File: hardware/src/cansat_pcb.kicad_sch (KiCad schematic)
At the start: 0 parts

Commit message: app advanced
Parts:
- added U1: XIAO-nRF52840-SMD, Seeed_Studio_XIAO_Series:XIAO-nRF52840-SMD, symbol Seeed_Studio_XIAO_Series-20240814:XIAO-nRF52840-SMD
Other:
- company: (none) -> Hydro Vinci
- title: (none) -> Cansat_pcb
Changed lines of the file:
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@@
 	(generator "eeschema")
 	(generator_version "9.0")
-	(paper "A4")
+	(paper "A3")
+	(title_block
+		(title "Cansat_pcb")
+		(date "2026-02-22")
+		(rev "Enzo Morin")
+		(company "Hydro Vinci")
+		(comment 1 "1st layer of the pcb in the cansat")
+	)
+	(rectangle
+		(start 12.7 12.7)
+		(end 151.13 142.24)
+		(stroke
+			(width 0)
+			(type default)
+			(color 194 0 0 1)
+		)
+		(fill
+			(type none)
+		)
+	)
+	(label "actuators/indicators"
+		(at 167.64 154.94 0)
+		(effects
+			(font
+				(size 4.27 4.27)
+			)
+			(justify left bottom)
+		)
+	)
+	(label "Main-part_microcontroler"
+		(at 15.24 21.59 0)
+		(effects
+			(font
+				(size 4.27 4.27)
+			)
+			(justify left bottom)
+		)
+	)
+	(label "storage and radio"
+		(at 226.06 25.4 0)
+		(effects
+			(font
+				(size 4.27 4.27)
+			)
+			(justify left bottom)
+		)
+	)
+	(label "alimentation"
+		(at 157.48 25.4 0)
+		(effects
+			(font
+				(size 4.27 4.27)
+			)
+			(justify left bottom)
+		)
+	)
+	(label "sensors"
+		(at 21.59 154.94 0)
+		(effects
+			(font
+				(size 4.27 4.27)
+			)
+			(justify left bottom)
+		)
+	)
+	(symbol
+		(lib_id "Seeed_Studio_XIAO_Series-20240814:XIAO-nRF52840-SMD")
+		(at 64.77 74.93 0)
+		(unit 1)
+		(exclude_from_sim no)
+		(in_bom yes)
+		(on_board yes)
+		(dnp no)
+		(fields_autoplaced yes)
+		(property "Reference" "U1"
+			(at 73.2633 49.53 0)
+			(effects
+				(font
+					(size 1.27 1.27)
+				)
+				(justify left)
+			)
+		)
+		(property "Value" "XIAO-nRF52840-SMD"
+			(at 73.2633 52.07 0)
+			(effects
+				(font
+					(size 1.27 1.27)
+				)
+				(justify left)
+			)
+		)
+		(property "Footprint" "Seeed_Studio_XIAO_Series:XIAO-nRF52840-SMD"
+			(at 55.88 69.85 0)
+			(effects
+				(font
+					(size 1.27 1.27)
+				)
+				(hide yes)
+			)
+		)
+		(property "Datasheet" ""
+			(at 55.88 69.85 0)
+			(effects
+				(font
+					(size 1.27 1.27)
+				)
+				(hide yes)
+			)
+		)
+		(property "Description" ""
+			(at 64.77 74.93 0)
+			(effects
+				(font
+					(size 1.27 1.27)
+				)
+				(hide yes)
+			)
+		)
+		(pin "18"
+		)
+		(pin "20"
+		)
+		(pin "22"
+		)
+		(pin "11"
+		)
+		(pin "4"
+		)
+		(pin "12"
+		)
+		(pin "15"
+		)
+		(pin "17"
+		)
+		(pin "16"
+		)
+		(pin "10"
+		)
+		(pin "8"
+		)
+		(pin "9"
+		)
+		(pin "19"
+		)
+		(pin "3"
+		)
+		(pin "2"
+		)
+		(pin "1"
+		)
+		(pin "5"
+		)
+		(pin "6"
+		)
+		(pin "7"
+		)
+		(pin "14"
+		)
+		(pin "21"
+		)
+		(pin "13"
+		)
+		(instances
+			(project ""
+				(path "/f7c433f5-979d-4748-9c6b-df3b09da91ad"
+					(reference "U1")
+					(unit 1)
+				)
+			)
+		)
+	)
 	(sheet_instances
 		(path "/"

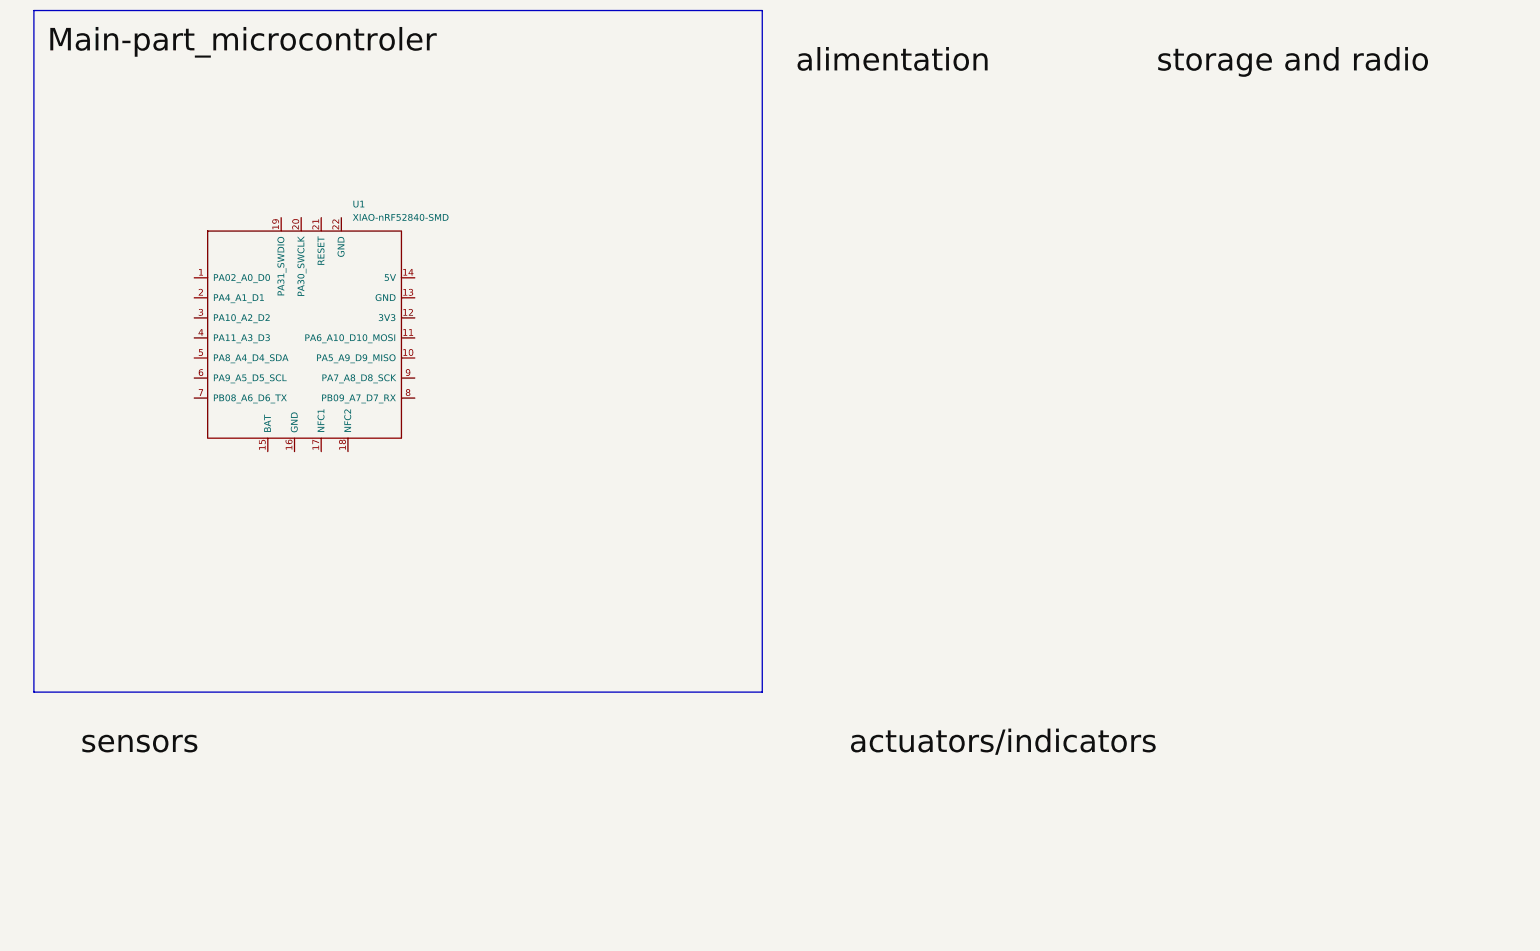
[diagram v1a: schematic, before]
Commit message: feature: add map on app + server change
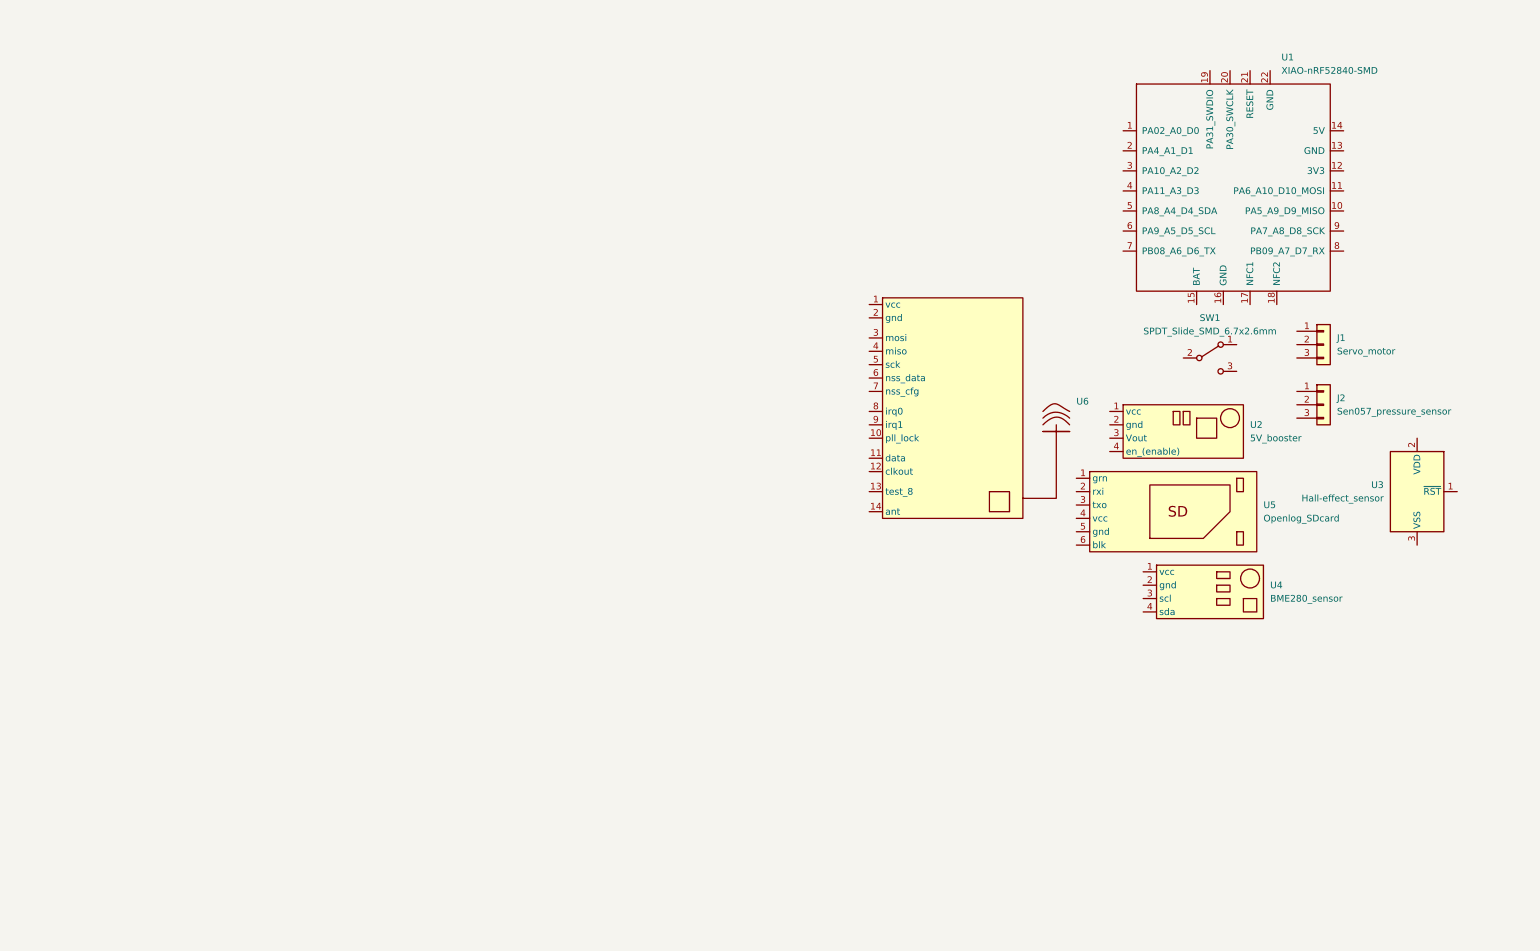
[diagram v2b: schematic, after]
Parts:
- added J1: Servo_motor, Connector_PinHeader_2.54mm:PinHeader_1x03_P2.54mm_Vertical, symbol Connector_Generic:Conn_01x03
- added J2: Sen057_pressure_sensor, Connector_PinHeader_2.54mm:PinHeader_1x03_P2.54mm_Vertical, symbol Connector_Generic:Conn_01x03
- added SW1: SPDT_Slide_SMD_6.7x2.6mm, PCM_SparkFun-Switch:Slide_SPST_SMD_6.7x2.6mm, symbol PCM_SparkFun-Switch:SPDT_Slide_SMD_6.7x2.6mm
- added U2: 5V_booster, symbol Enzo's_library:Aadafruit_5V_booster
- added U3: Hall-effect_sensor, Package_TO_SOT_THT:TO-92_Inline, symbol Power_Supervisor:MCP120-xxxDxTO
- added U4: BME280_sensor, symbol Enzo's_library:BME_280
- added U5: Openlog_SDcard, symbol Enzo's_library:Openlog_SDcard
- added U6: ~, symbol Enzo's_library:E23-433m13S_rf-module
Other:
- moved on the sheet: U1

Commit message: refactor: final app structure
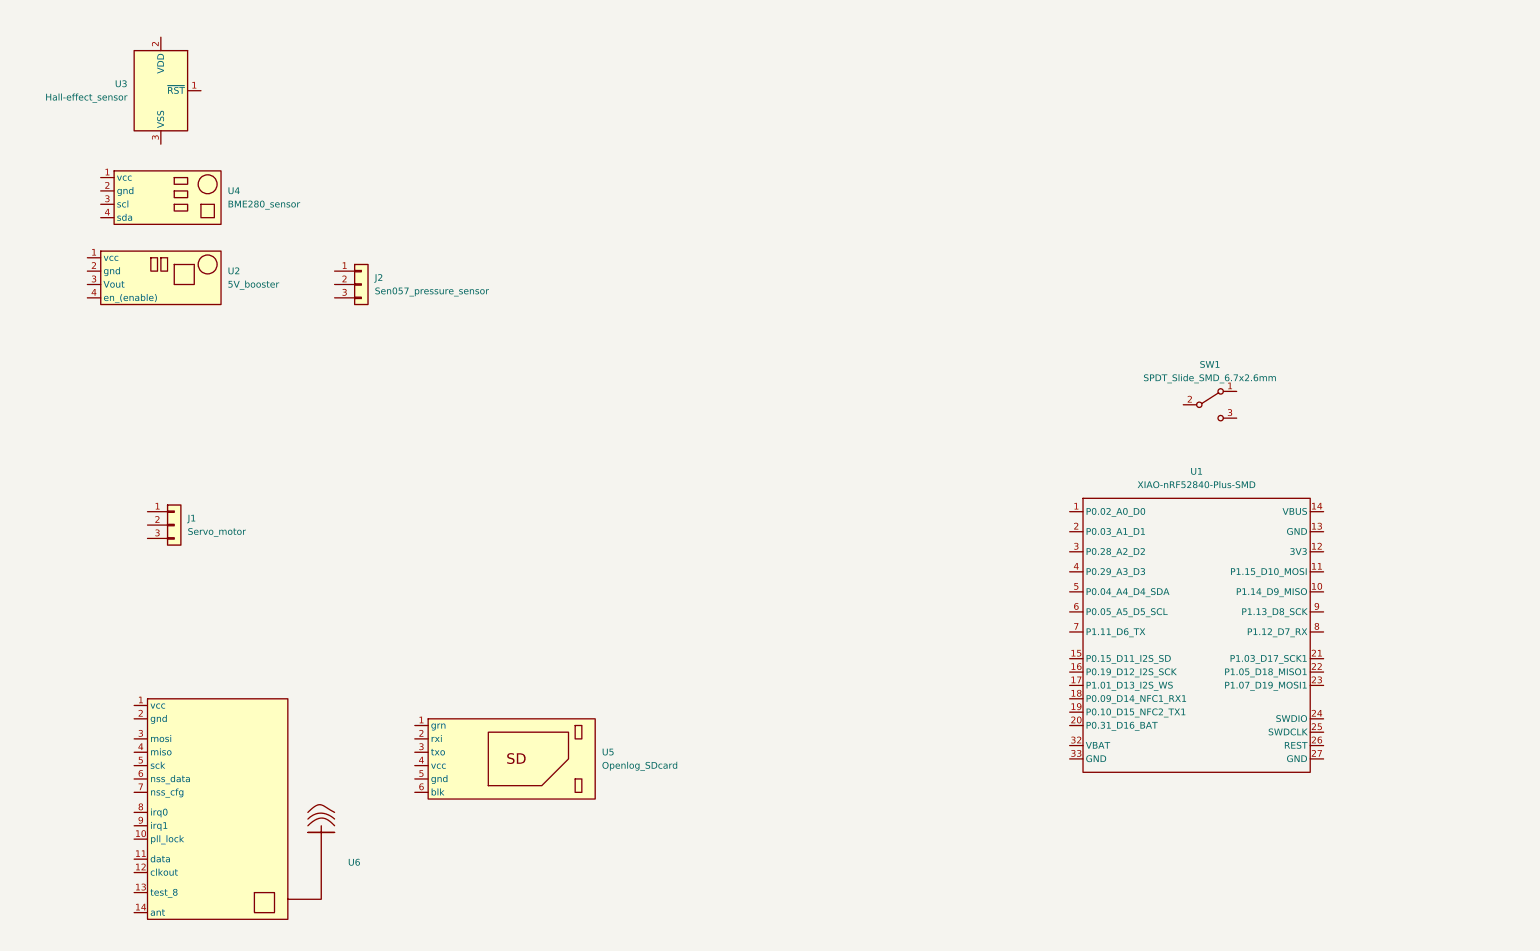
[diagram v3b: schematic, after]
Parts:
- removed U1: XIAO-nRF52840-SMD, Seeed_Studio_XIAO_Series:XIAO-nRF52840-SMD, symbol Seeed_Studio_XIAO_Series-20240814:XIAO-nRF52840-SMD
- added U1: XIAO-nRF52840-Plus-SMD, XIAO_Series_Footprints:XIAO-nRF52840-Plus-SMD, symbol Seeed_Studio_XIAO_Series:XIAO-nRF52840_Plus_SMD
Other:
- moved on the sheet: J1, J2, SW1, U2, U3, U4, U5, U6

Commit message: feature: pcb started
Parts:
- removed U3: Hall-effect_sensor, Package_TO_SOT_THT:TO-92_Inline, symbol Power_Supervisor:MCP120-xxxDxTO
- added BZ1: Buzzer_info, Buzzer_Beeper:Buzzer_12x9.5RM7.6, symbol Device:Buzzer
- added J3: Hall_effect_sensor, Connector_PinHeader_2.54mm:PinHeader_1x03_P2.54mm_Vertical, symbol Connector_Generic:Conn_01x03
- added J4: Jack plug, Connector_PinHeader_1.00mm:PinHeader_1x02_P1.00mm_Horizontal, symbol Connector_Generic:Conn_01x02
- added SW2: telemetry_btn, craby's_library:SW_BUTT-2, symbol Switch:SW_MEC_5G
- SW1: footprint PCM_SparkFun-Switch:Slide_SPST_SMD_6.7x2.6mm -> Button_Switch_SMD:SW_SPDT_CK_JS102011SAQN
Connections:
- new net: SW2.1 (A), SW2.2 (A)
- new net: SW2.3 (B), SW2.4 (B)
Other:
- moved on the sheet: J1, J2, SW1, U1, U2, U4, U5, U6

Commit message: feature: add some componants to the pcb
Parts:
- J4: footprint Connector_PinHeader_1.00mm:PinHeader_1x02_P1.00mm_Horizontal -> Connector_PinHeader_2.54mm:PinHeader_1x02_P2.54mm_Horizontal
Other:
- moved on the sheet: BZ1
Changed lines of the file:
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@@
 			)
 		)
-		(property "Footprint" "Connector_PinHeader_1.00mm:PinHeader_1x02_P1.00mm_Horizontal"
+		(property "Footprint" "Connector_PinHeader_2.54mm:PinHeader_1x02_P2.54mm_Horizontal"
 			(at 127 144.78 0)
 			(effects
@@
 	(symbol
 		(lib_id "Device:Buzzer")
-		(at 144.78 163.83 0)
+		(at 91.44 27.94 0)
 		(unit 1)
 		(exclude_from_sim no)
@@
 		(fields_autoplaced yes)
 		(property "Reference" "BZ1"
-			(at 148.59 162.5599 0)
+			(at 95.25 26.6699 0)
 			(effects
 				(font
@@
 		)
 		(property "Value" "Buzzer_info"
-			(at 148.59 165.0999 0)
+			(at 95.25 29.2099 0)
 			(effects
 				(font
@@
 		)
 		(property "Footprint" "Buzzer_Beeper:Buzzer_12x9.5RM7.6"
-			(at 144.145 161.29 90)
+			(at 90.805 25.4 90)
 			(effects
 				(font
@@
 		)
 		(property "Datasheet" "~"
-			(at 144.145 161.29 90)
+			(at 90.805 25.4 90)
 			(effects
 				(font
@@
 		)
 		(property "Description" "Buzzer, polarized"
-			(at 144.78 163.83 0)
-			(effects
-				(font
+			(at 91.44 27.94 0)
+			(effects
+				(font
